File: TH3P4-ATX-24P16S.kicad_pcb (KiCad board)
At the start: 2 copper layers, 51.8 x 23.2 mm, 2 parts, among them J1 ATX_24pin_female_solder, J2 ATX_16pin_male

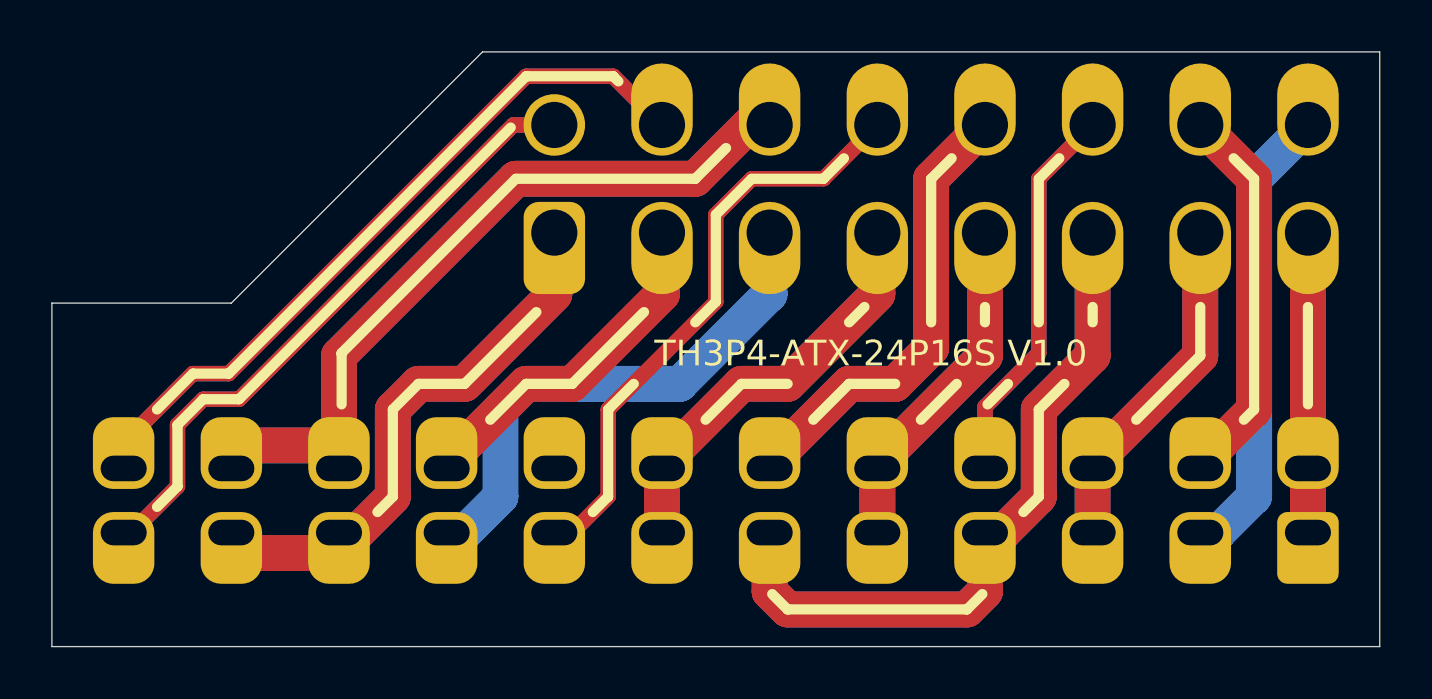
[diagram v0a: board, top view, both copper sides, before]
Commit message: Updated with real life experiences
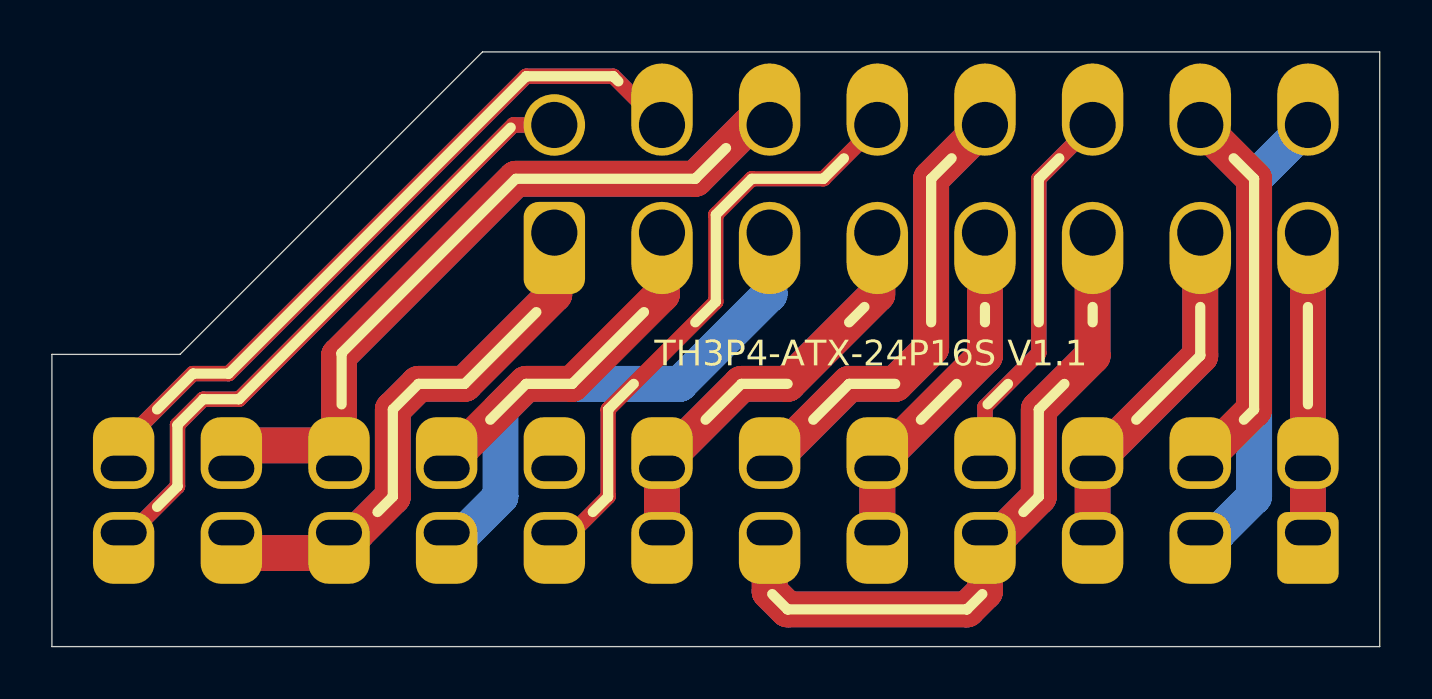
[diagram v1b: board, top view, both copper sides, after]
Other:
- outline, holes or cut-outs redrawn
- board text added: "TH3P4-ATX-24P16S V1.1"
- board text removed: "TH3P4-ATX-24P16S V1.0"
